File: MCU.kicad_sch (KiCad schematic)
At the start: 0 parts

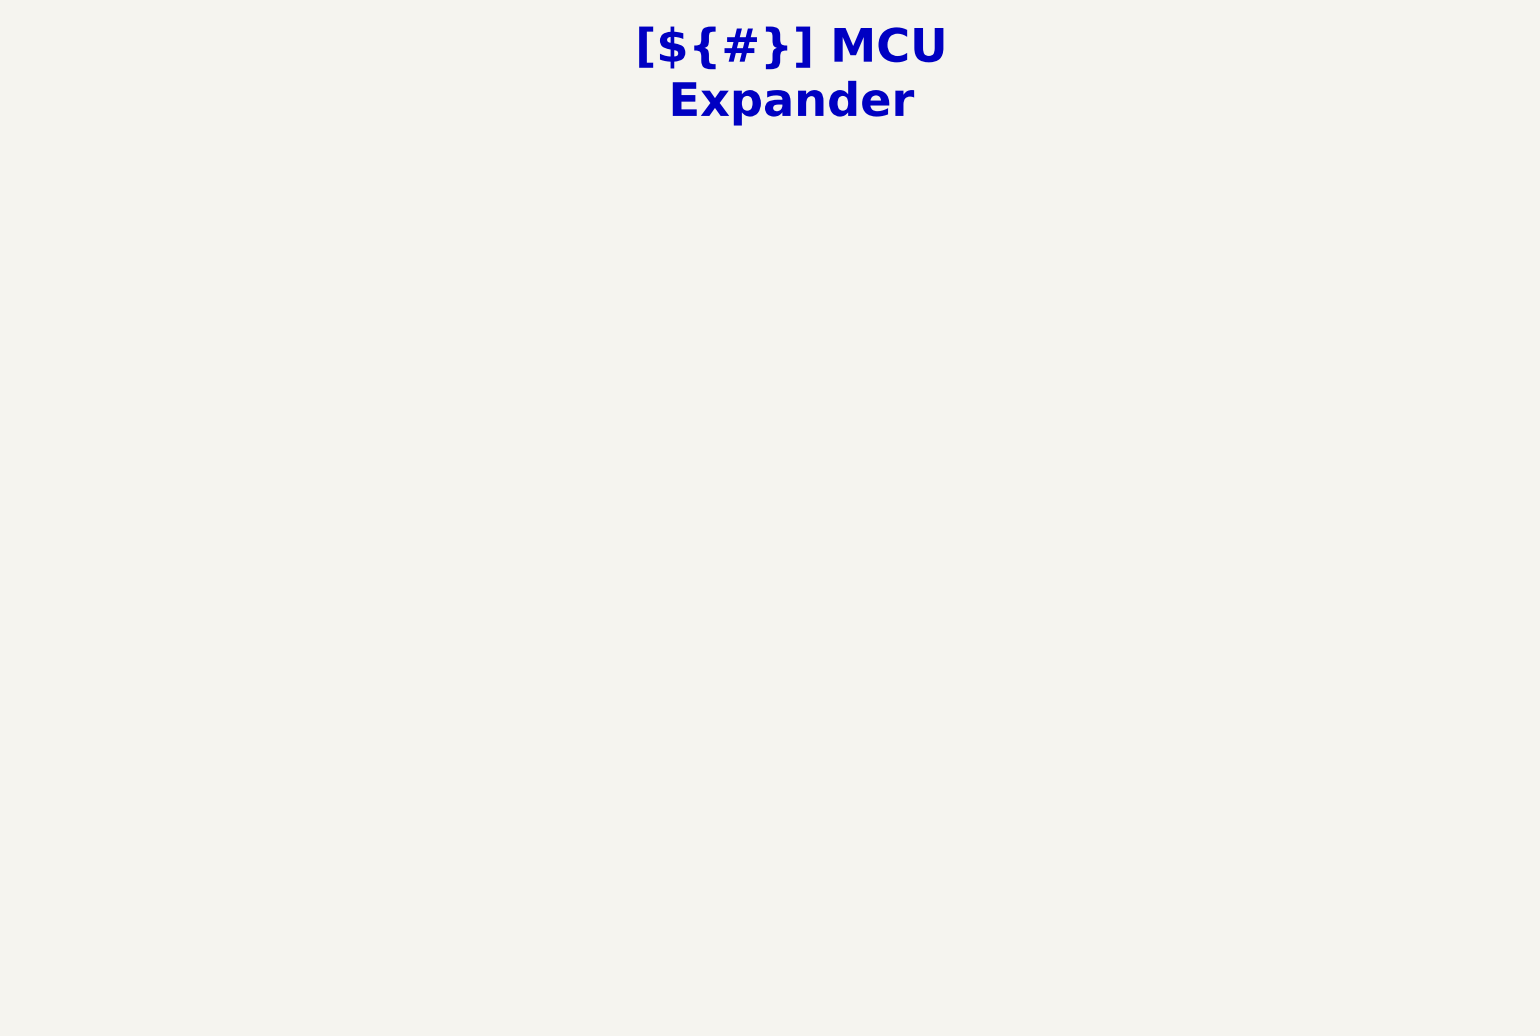
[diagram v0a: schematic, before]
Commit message: [Schematic][Add] MCU
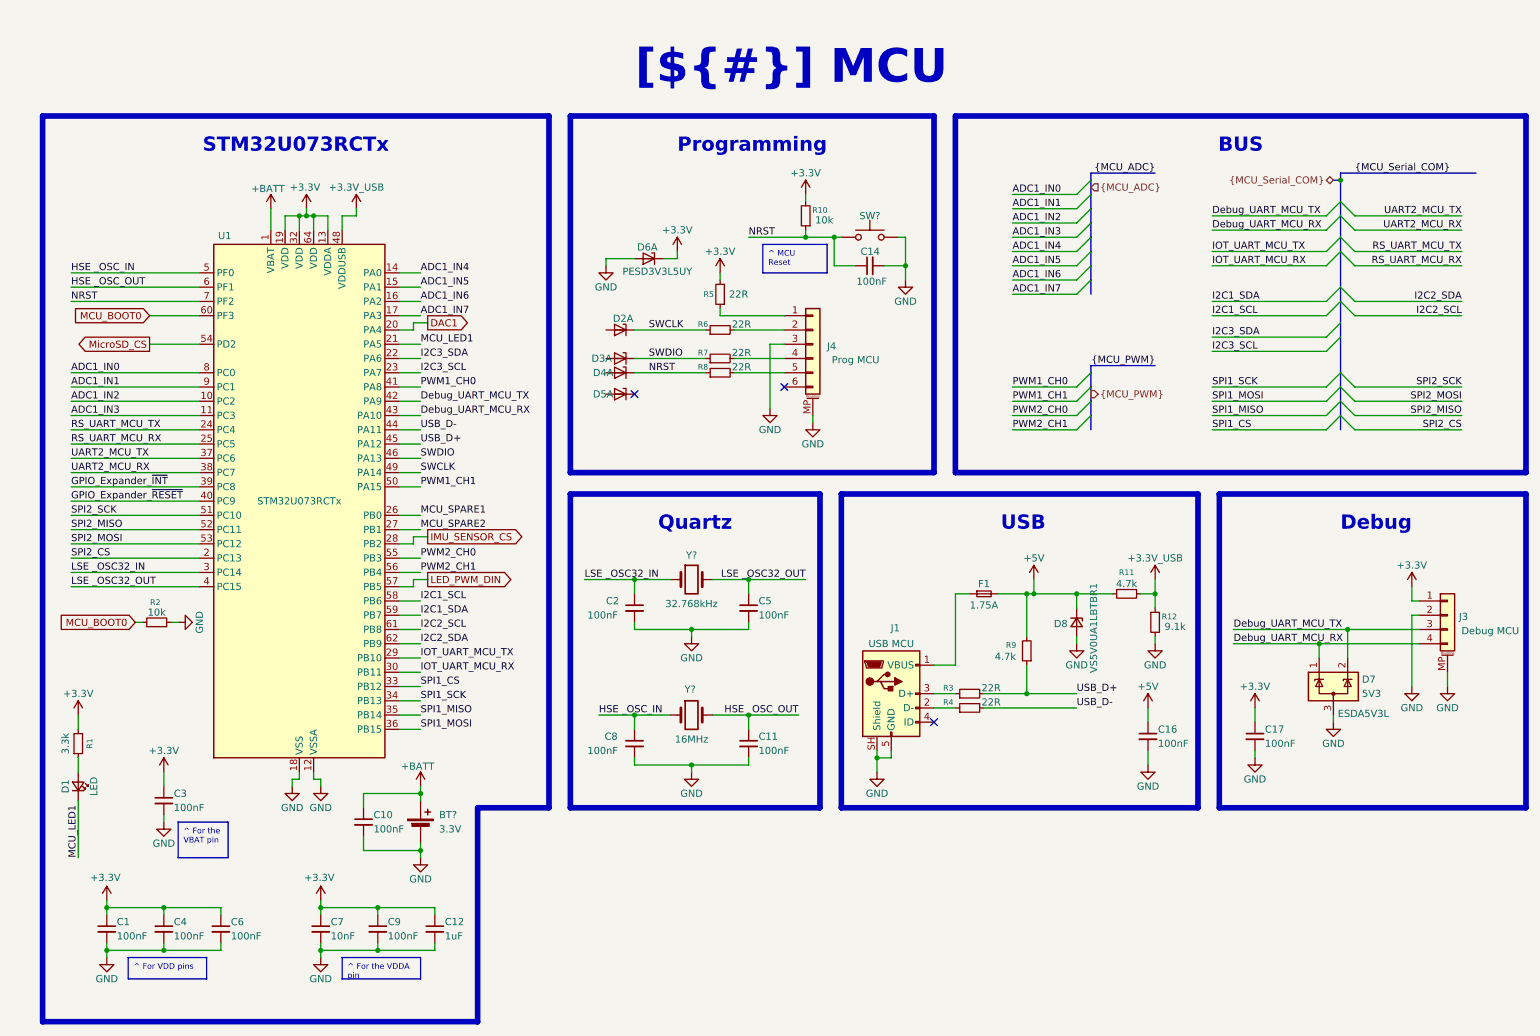
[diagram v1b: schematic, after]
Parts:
- added BT?: 3.3V, Battery:BatteryHolder_Keystone_103_1x20mm, symbol Device:Battery_Cell
- added C1, C10, C11, C14, C16, C17, C2, C3, C4, C5, C6, C8, C9: 100nF, Capacitor_SMD:C_0603_1608Metric_Pad1.08x0.95mm_HandSolder, symbol Device:C_Small
- added C12: 1uF, Capacitor_SMD:C_0603_1608Metric_Pad1.08x0.95mm_HandSolder, symbol Device:C_Small
- added C7: 10nF, Capacitor_SMD:C_0603_1608Metric_Pad1.08x0.95mm_HandSolder, symbol Device:C_Small
- added D1: 5V, LED_SMD:LED_0805_2012Metric_Pad1.15x1.40mm_HandSolder, symbol Device:LED_Small
- added D2, D3, D4, D5, D6: 3.3V, Package_TO_SOT_SMD:SOT-363_SC-70-6, symbol Power_Protection:PESD3V3L5UY
- added D7: 5V3, Package_TO_SOT_SMD:SOT-23-3, symbol Power_Protection:ESDA5V3L
- added D8: 5V, Diode_SMD:D_SMB, symbol Device:D_Zener_Small
- added F1: 1.75A, Fuse:Fuse_0603_1608Metric, symbol Device:Fuse_Small
- added J1: *, Connector_USB:USB_B_Amphenol_MUSB-D511_Vertical_Rugged, symbol Connector:USB_B_Micro
- added J3: *, Connector_JST:JST_ZH_S4B-ZR-SM4A-TF_1x04-1MP_P1.50mm_Horizontal, symbol Connector_Generic_MountingPin:Conn_01x04_MountingPin
- added J4: *, Connector_JST:JST_ZH_S6B-ZR-SM4A-TF_1x06-1MP_P1.50mm_Horizontal, symbol Connector_Generic_MountingPin:Conn_01x06_MountingPin
- added R1: 3.3k, Resistor_SMD:R_0603_1608Metric_Pad0.98x0.95mm_HandSolder, symbol Device:R_Small
- added R10, R2: 10k, Resistor_SMD:R_0603_1608Metric_Pad0.98x0.95mm_HandSolder, symbol Device:R_Small
- added R11: 4.7k, Resistor_SMD:R_0805_2012Metric_Pad1.20x1.40mm_HandSolder, symbol Device:R_Small
- added R12: 9.1k, Resistor_SMD:R_0805_2012Metric_Pad1.20x1.40mm_HandSolder, symbol Device:R_Small
- added R3, R4, R5, R6, R7, R8: 22R, Resistor_SMD:R_0603_1608Metric_Pad0.98x0.95mm_HandSolder, symbol Device:R_Small
- added R9: 4.7k, Resistor_SMD:R_0603_1608Metric_Pad0.98x0.95mm_HandSolder, symbol Device:R_Small
- added SW?: *, Button_Switch_SMD:SW_SPST_CK_RS282G05A3, symbol Switch:SW_Push
- added U1: *, Package_QFP:LQFP-64_10x10mm_P0.5mm, symbol MCU_ST_STM32U0:STM32U073RCTx
- added Y?: 32.768kHz, Crystal:Crystal_SMD_2012-2Pin_2.0x1.2mm, symbol Device:Crystal
- added Y?: 16MHz, Crystal:Crystal_SMD_2012-2Pin_2.0x1.2mm, symbol Device:Crystal
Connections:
- new net: J1.3 (D+), R3.1
- new net: J4.1 (Pin_1), R5.1
- new net: J4.2 (Pin_2), R6.2
- new net: J4.4 (Pin_4), R7.2
- new net: J4.5 (Pin_5), R8.2
- new net: D1.2 (A), R1.1
- new net: F1.1, J1.1 (VBUS)
- new net: J1.2 (D-), R4.1
- new net +3.3V: C1.1, C12.1, C17.1, C3.1, C4.1, C6.1, C7.1, C9.1, D6.1 (K1), J3.1 (Pin_1), R1.2, R10.2, R5.2, U1.13 (VDDA), U1.19 (VDD), U1.32 (VDD), U1.64 (VDD)
- new net +3.3V_USB: R11.1, R12.1, U1.48 (VDDUSB)
- new net +5V: C16.1, D8.1 (K), F1.2, R11.2, R9.2
- new net +BATT: BT?.1 (+), C10.1, U1.1 (VBAT)
- new net ADC1_IN0: U1.8 (PC0)
- new net ADC1_IN1: U1.9 (PC1)
- new net ADC1_IN2: U1.10 (PC2)
- new net ADC1_IN3: U1.11 (PC3)
- new net ADC1_IN4: U1.14 (PA0)
- new net ADC1_IN5: U1.15 (PA1)
- new net ADC1_IN6: U1.16 (PA2)
- new net ADC1_IN7: U1.17 (PA3)
- new net DAC1: U1.20 (PA4)
- new net Debug_UART_MCU_RX: D7.1 (K), J3.4 (Pin_4), U1.43 (PA10)
- new net Debug_UART_MCU_TX: D7.2 (K), J3.3 (Pin_3), U1.42 (PA9)
- new net GND: BT?.2 (-), C1.2, C10.2, C11.2, C12.2, C14.2, C16.2, C17.2, C2.2, C3.2, C4.2, C5.2, C6.2, C7.2, C8.2, C9.2, D6.2 (A), D7.3 (A), D8.2 (A), J1.5 (GND), J1.SH (Shield), J3.2 (Pin_2), J3.MP (MountPin), J4.3 (Pin_3), J4.MP (MountPin), R12.2, R2.2, SW?.2, U1.12 (VSSA), U1.18 (VSS), U1.31 (VSS), U1.47 (VSS), U1.63 (VSS)
- new net GPIO_Expander_~{INT}: U1.39 (PC8)
- new net GPIO_Expander_~{RESET}: U1.40 (PC9)
- new net HSE _OSC_IN: C8.1, U1.5 (PF0), Y?.1
- new net HSE _OSC_OUT: C11.1, U1.6 (PF1), Y?.2
- new net I2C1_SCL: U1.58 (PB6)
- new net I2C1_SDA: U1.59 (PB7)
- new net I2C2_SCL: U1.61 (PB8)
- new net I2C2_SDA: U1.62 (PB9)
- new net I2C3_SCL: U1.23 (PA7)
- new net I2C3_SDA: U1.22 (PA6)
- new net IMU_SENSOR_CS: U1.28 (PB2)
- new net IOT_UART_MCU_RX: U1.30 (PB11)
- new net IOT_UART_MCU_TX: U1.29 (PB10)
- new net LED_PWM_DIN: U1.57 (PB5)
- new net LSE _OSC32_IN: C2.1, U1.3 (PC14), Y?.1
- new net LSE _OSC32_OUT: C5.1, U1.4 (PC15), Y?.2
- new net MCU_BOOT0: R2.1, U1.60 (PF3)
- new net MCU_LED1: D1.1 (K), U1.21 (PA5)
- new net MCU_SPARE1: U1.26 (PB0)
- new net MCU_SPARE2: U1.27 (PB1)
- new net MicroSD_CS: U1.54 (PD2)
- new net NRST: C14.1, D4.1 (K1), R10.1, R8.1, SW?.1, U1.7 (PF2)
- new net PWM1_CH0: U1.41 (PA8)
- new net PWM1_CH1: U1.50 (PA15)
- new net PWM2_CH0: U1.55 (PB3)
- new net PWM2_CH1: U1.56 (PB4)
- new net RS_UART_MCU_RX: U1.25 (PC5)
- new net RS_UART_MCU_TX: U1.24 (PC4)
- new net SPI1_CS: U1.33 (PB12)
- new net SPI1_MISO: U1.35 (PB14)
- new net SPI1_MOSI: U1.36 (PB15)
- new net SPI1_SCK: U1.34 (PB13)
- new net SPI2_CS: U1.2 (PC13)
- new net SPI2_MISO: U1.52 (PC11)
- new net SPI2_MOSI: U1.53 (PC12)
- new net SPI2_SCK: U1.51 (PC10)
- new net SWCLK: D2.1 (K1), R6.1, U1.49 (PA14)
- new net SWDIO: D3.1 (K1), R7.1, U1.46 (PA13)
- new net UART2_MCU_RX: U1.38 (PC7)
- new net UART2_MCU_TX: U1.37 (PC6)
- new net USB_D+: R3.2, R9.1, U1.45 (PA12)
- new net USB_D-: R4.2, U1.44 (PA11)
- no-connect marks 0 -> 3
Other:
- title: MCU Expander -> MCU

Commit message: [Schematic][Add] MCU Expander Schematic
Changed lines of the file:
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@@
 	(wire
 		(pts
+			(xy 82.55 100.33) (xy 82.55 99.06)
+		)
+		(stroke
+			(width 0)
+			(type default)
+		)
+	)
+	(wire
+		(pts
 			(xy 121.92 135.89) (xy 121.92 138.43)
 		)
@@
 	(wire
 		(pts
+			(xy 43.18 95.25) (xy 44.45 95.25)
+		)
+		(stroke
+			(width 0)
+			(type default)
+		)
+	)
+	(wire
+		(pts
 			(xy 250.19 55.88) (xy 269.24 55.88)
 		)
@@
 	(wire
 		(pts
+			(xy 82.55 102.87) (xy 82.55 101.6)
+		)
+		(stroke
+			(width 0)
+			(type default)
+		)
+	)
+	(wire
+		(pts
 			(xy 170.18 50.8) (xy 168.91 50.8)
 		)
@@
 	(wire
 		(pts
+			(xy 82.55 101.6) (xy 85.09 101.6)
+		)
+		(stroke
+			(width 0)
+			(type default)
+		)
+	)
+	(wire
+		(pts
 			(xy 260.35 113.03) (xy 260.35 115.57)
 		)
@@
 	(wire
 		(pts
+			(xy 82.55 99.06) (xy 85.09 99.06)
+		)
+		(stroke
+			(width 0)
+			(type default)
+		)
+	)
+	(wire
+		(pts
+			(xy 41.91 93.98) (xy 43.18 93.98)
+		)
+		(stroke
+			(width 0)
+			(type default)
+		)
+	)
+	(wire
+		(pts
 			(xy 80.01 128.27) (xy 83.82 128.27)
 		)
@@
 	(wire
 		(pts
-			(xy 21.59 97.79) (xy 44.45 97.79)
+			(xy 41.91 96.52) (xy 43.18 96.52)
 		)
 		(stroke
@@
 	(wire
 		(pts
+			(xy 43.18 93.98) (xy 43.18 95.25)
+		)
+		(stroke
+			(width 0)
+			(type default)
+		)
+	)
+	(wire
+		(pts
 			(xy 38.1 170.18) (xy 38.1 171.45)
 		)
@@
 	(wire
 		(pts
+			(xy 43.18 97.79) (xy 44.45 97.79)
+		)
+		(stroke
+			(width 0)
+			(type default)
+		)
+	)
+	(wire
+		(pts
 			(xy 116.84 54.61) (xy 116.84 55.88)
 		)
@@
 	(wire
 		(pts
-			(xy 80.01 102.87) (xy 83.82 102.87)
+			(xy 80.01 102.87) (xy 82.55 102.87)
 		)
 		(stroke
@@
 	(wire
 		(pts
-			(xy 21.59 95.25) (xy 44.45 95.25)
-		)
-		(stroke
-			(width 0)
-			(type default)
-		)
-	)
-	(wire
-		(pts
 			(xy 66.04 168.91) (xy 66.04 170.18)
 		)
@@
 	(wire
 		(pts
-			(xy 80.01 100.33) (xy 83.82 100.33)
+			(xy 80.01 100.33) (xy 82.55 100.33)
 		)
 		(stroke
@@
 	(wire
 		(pts
+			(xy 43.18 96.52) (xy 43.18 97.79)
+		)
+		(stroke
+			(width 0)
+			(type default)
+		)
+	)
+	(wire
+		(pts
 			(xy 152.4 43.18) (xy 152.4 44.45)
 		)
@@
 		)
 	)
-	(label "GPIO_Expander_~{INT}"
-		(at 21.59 95.25 0)
-		(effects
-			(font
-				(size 1.27 1.27)
-			)
-			(justify left bottom)
-		)
-	)
 	(label "Debug_UART_MCU_TX"
 		(at 224.79 46.99 0)
@@
 		)
 	)
-	(label "GPIO_Expander_~{RESET}"
-		(at 21.59 97.79 0)
-		(effects
-			(font
-				(size 1.27 1.27)
-			)
-			(justify left bottom)
-		)
-	)
 	(label "SPI2_MOSI"
 		(at 21.59 105.41 0)
@@
 		)
 	)
-	(label "MCU_SPARE1"
-		(at 83.82 100.33 0)
-		(effects
-			(font
-				(size 1.27 1.27)
-			)
-			(justify left bottom)
-		)
-	)
 	(label "SPI2_SCK"
 		(at 269.24 77.47 180)
@@
 		)
 	)
-	(label "MCU_SPARE2"
-		(at 83.82 102.87 0)
-		(effects
-			(font
-				(size 1.27 1.27)
-			)
-			(justify left bottom)
-		)
-	)
 	(label "I2C3_SCL"
 		(at 83.82 74.93 0)
@@
 		)
 	)
+	(global_label "GPIO_Expander_~{INT}"
+		(shape input)
+		(at 41.91 93.98 180)
+		(fields_autoplaced yes)
+		(effects
+			(font
+				(size 1.27 1.27)
+			)
+			(justify right)
+		)
+		(property "Intersheetrefs" "${INTERSHEET_REFS}"
+			(at 20.9635 93.98 0)
+			(effects
+				(font
+					(size 1.27 1.27)
+				)
+				(justify right)
+				(hide yes)
+			)
+		)
+	)
+	(global_label "MCU_SPARE1"
+		(shape bidirectional)
+		(at 85.09 99.06 0)
+		(fields_autoplaced yes)
+		(effects
+			(font
+				(size 1.27 1.27)
+			)
+			(justify left)
+		)
+		(property "Intersheetrefs" "${INTERSHEET_REFS}"
+			(at 100.2913 99.06 0)
+			(effects
+				(font
+					(size 1.27 1.27)
+				)
+				(justify left)
+				(hide yes)
+			)
+		)
+	)
 	(global_label "MCU_BOOT0"
 		(shape input)
@@
 		)
 	)
+	(global_label "GPIO_Expander_~{RESET}"
+		(shape input)
+		(at 41.91 96.52 180)
+		(fields_autoplaced yes)
+		(effects
+			(font
+				(size 1.27 1.27)
+			)
+			(justify right)
+		)
+		(property "Intersheetrefs" "${INTERSHEET_REFS}"
+			(at 18.1213 96.52 0)
+			(effects
+				(font
+					(size 1.27 1.27)
+				)
+				(justify right)
+				(hide yes)
+			)
+		)
+	)
 	(global_label "DAC1"
 		(shape output)
@@
 			(effects
 				(font
+					(size 1.27 1.27)
+				)
+				(justify left)
+				(hide yes)
+			)
+		)
+	)
+	(global_label "MCU_SPARE2"
+		(shape bidirectional)
+		(at 85.09 101.6 0)
+		(fields_autoplaced yes)
+		(effects
+			(font
+				(size 1.27 1.27)
+			)
+			(justify left)
+		)
+		(property "Intersheetrefs" "${INTERSHEET_REFS}"
+			(at 101.4026 101.6 0)
+			(effects
+				(font

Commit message: [Schematic][Modify] Clear all annotation
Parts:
- renumbered C4 to C?, C1 to C?, C10 to C?, C17 to C?, C8 to C?, C16 to C?, C12 to C?, C14 to C?, C11 to C?, C6 to C?, C2 to C?, C3 to C?, C5 to C?, C9 to C?, C7 to C?, D4 to D?, D7 to D?, D8 to D?, D3 to D?, D6 to D?, D5 to D?, D2 to D?, D1 to D?, F1 to F?, J4 to J?, J3 to J?, J1 to J?, R3 to R?, R5 to R?, R1 to R?, R4 to R?, R9 to R?, R10 to R?, R11 to R?, R7 to R?, R6 to R?, R12 to R?, R2 to R?, R8 to R?, U1 to U?

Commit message: [Schematic][Modify] Modification of the TVD programming Diode
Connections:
- net NRST: now also D?.5 (K4); no longer D?.1 (K1)
- net SWCLK: now also D?.3 (K2); no longer D?.1 (K1)
- net SWDIO: now also D?.4 (K3); no longer D?.1 (K1)
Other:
- moved on the sheet: D?A
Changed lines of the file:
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@@
 		(exclude_from_sim no)
 		(at 227.33 97.6497 0)
-		(size 53.34 7.7603)
+		(size 52.07 7.7603)
 		(margins 1.9049 1.9049 1.9049 1.9049)
 		(stroke
@@
 	(wire
 		(pts
-			(xy 129.54 54.61) (xy 129.54 53.34)
-		)
-		(stroke
-			(width 0)
-			(type default)
-		)
-	)
-	(wire
-		(pts
 			(xy 80.01 118.11) (xy 83.82 118.11)
 		)
@@
 	(wire
 		(pts
-			(xy 121.92 54.61) (xy 116.84 54.61)
+			(xy 118.11 53.34) (xy 118.11 57.15)
 		)
 		(stroke
@@
 	(wire
 		(pts
-			(xy 127 54.61) (xy 129.54 54.61)
+			(xy 118.11 48.26) (xy 118.11 44.45)
 		)
 		(stroke
@@
 	(wire
 		(pts
-			(xy 116.84 54.61) (xy 116.84 55.88)
-		)
-		(stroke
-			(width 0)
-			(type default)
-		)
-	)
-	(wire
-		(pts
 			(xy 165.1 143.51) (xy 165.1 146.05)
 		)
@@
 		(lib_id "Power_Protection:PESD3V3L5UY")
 		(at 119.38 74.93 180)
-		(unit 1)
+		(unit 4)
 		(exclude_from_sim no)
 		(in_bom yes)
@@
 		(dnp no)
 		(property "Reference" "D?"
-			(at 116.332 74.93 0)
+			(at 116.078 74.93 0)
 			(effects
 				(font
@@
 				(path "/f9e05184-c88b-4a88-ae9c-ab2bdb32be7c/c5103ceb-5325-4a84-a025-9638a412984e/8566d017-436e-49aa-b68c-18b49ef4128b"
 					(reference "D?")
-					(unit 1)
+					(unit 4)
 				)
 			)
@@
 		(lib_id "Power_Protection:PESD3V3L5UY")
 		(at 119.38 72.39 180)
-		(unit 1)
+		(unit 3)
 		(exclude_from_sim no)
 		(in_bom yes)
@@
 				(path "/f9e05184-c88b-4a88-ae9c-ab2bdb32be7c/c5103ceb-5325-4a84-a025-9638a412984e/8566d017-436e-49aa-b68c-18b49ef4128b"
 					(reference "D?")
-					(unit 1)
+					(unit 3)
 				)
 			)
@@
 		(dnp no)
 		(property "Reference" "C?"
-			(at 165.608 53.34 90)
+			(at 165.1 53.086 90)
 			(effects
 				(font
@@
 	(symbol
 		(lib_id "power:+3.3V")
-		(at 129.54 53.34 0)
+		(at 118.11 44.45 0)
 		(unit 1)
 		(exclude_from_sim no)
@@
 		(dnp no)
 		(property "Reference" "#PWR?"
-			(at 129.54 57.15 0)
+			(at 118.11 48.26 0)
 			(effects
 				(font
@@
 		)
 		(property "Value" "+3.3V"
-			(at 129.54 49.53 0)
+			(at 118.11 40.64 0)
 			(effects
 				(font
@@
 		)
 		(property "Footprint" ""
-			(at 129.54 53.34 0)
+			(at 118.11 44.45 0)
 			(effects
 				(font
@@
 		)
 		(property "Datasheet" ""
-			(at 129.54 53.34 0)
+			(at 118.11 44.45 0)
 			(effects
 				(font
@@
 		)
 		(property "Description" "Power symbol creates a global label with name \"+3.3V\""
-			(at 129.54 53.34 0)
+			(at 118.11 44.45 0)
 			(effects
 				(font
@@
 	(symbol
 		(lib_id "Power_Protection:PESD3V3L5UY")
-		(at 124.46 54.61 180)
+		(at 118.11 50.8 270)
 		(unit 1)
 		(exclude_from_sim no)
@@
 		(dnp no)
 		(property "Reference" "D?"
-			(at 124.206 52.578 0)
+			(at 116.078 51.054 0)
 			(effects
 				(font
@@
 		)
 		(property "Value" "3.3V"
-			(at 124.46 50.8 0)
+			(at 114.3 50.8 0)
 			(effects
 				(font
@@
 		)
 		(property "Footprint" "Package_TO_SOT_SMD:SOT-363_SC-70-6"
-			(at 124.46 59.69 0)
+			(at 123.19 50.8 0)
 			(effects
 				(font
@@
 		)
 		(property "Datasheet" "https://assets.nexperia.com/documents/data-sheet/PESDXL5UF_V_Y.pdf"
-			(at 124.46 49.53 0)
+			(at 113.03 50.8 0)
 			(effects
 				(font
@@
 		)
 		(property "Description" "Low capacitance unidirectional fivefold ESD protection diode array, 3.3V, Common Anode, SOT-363"
-			(at 124.46 54.61 0)
+			(at 118.11 50.8 0)
 			(effects
 				(font
@@
 		)
 		(property "PartNumber" "PESD3V3L5UY"
-			(at 125.984 56.896 0)
+			(at 120.396 49.276 0)
 			(effects
 				(font
@@
 		)
 		(property "PackageReference" "SOT-363"
-			(at 124.46 54.61 0)
+			(at 118.11 50.8 0)
 			(effects
 				(font
@@
 		)
 		(property "Manufacturer" "Nexperia"
-			(at 124.46 54.61 0)
+			(at 118.11 50.8 0)
 			(effects
 				(font
@@
 		)
 		(property "Comment" "ESD Diode"
-			(at 124.46 54.61 0)
+			(at 118.11 50.8 0)
 			(effects
 				(font
@@
 		(lib_id "Power_Protection:PESD3V3L5UY")
 		(at 119.38 78.74 180)
-		(unit 1)
+		(unit 5)
 		(exclude_from_sim no)
 		(in_bom yes)
@@
 		(dnp no)
 		(property "Reference" "D?"
-			(at 116.332 78.74 0)
+			(at 116.078 78.74 0)
 			(effects
 				(font
@@
 				(path "/f9e05184-c88b-4a88-ae9c-ab2bdb32be7c/c5103ceb-5325-4a84-a025-9638a412984e/8566d017-436e-49aa-b68c-18b49ef4128b"
 					(reference "D?")
-					(unit 1)
+					(unit 5)
 				)
 			)
@@
 		(lib_id "Power_Protection:PESD3V3L5UY")
 		(at 119.38 67.31 180)
-		(unit 1)
+		(unit 2)
 		(exclude_from_sim no)
 		(in_bom yes)
@@
 		(dnp no)
 		(property "Reference" "D?"
-			(at 119.888 65.278 0)
+			(at 116.078 67.31 0)
 			(effects
 				(font
@@
 				(path "/f9e05184-c88b-4a88-ae9c-ab2bdb32be7c/c5103ceb-5325-4a84-a025-9638a412984e/8566d017-436e-49aa-b68c-18b49ef4128b"
 					(reference "D?")
-					(unit 1)
+					(unit 2)
 				)
 			)
@@
 	(symbol
 		(lib_id "power:GND")
-		(at 116.84 55.88 0)
+		(at 118.11 57.15 0)
 		(unit 1)
 		(exclude_from_sim no)
@@
 		(dnp no)
 		(property "Reference" "#PWR?"
-			(at 116.84 62.23 0)
+			(at 118.11 63.5 0)
 			(effects
 				(font
@@
 		)
 		(property "Value" "GND"
-			(at 116.84 59.69 0)
+			(at 118.11 60.96 0)
 			(effects
 				(font
@@
 		)
 		(property "Footprint" ""
-			(at 116.84 55.88 0)
+			(at 118.11 57.15 0)
 			(effects
 				(font
@@
 		)
 		(property "Datasheet" ""
-			(at 116.84 55.88 0)
+			(at 118.11 57.15 0)
 			(effects
 				(font
@@
 		)
 		(property "Description" "Power symbol creates a global label with name \"GND\" , ground"
-			(at 116.84 55.88 0)
+			(at 118.11 57.15 0)
 			(effects
 				(font

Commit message: [Schematic][Modify] Annotation of all  the components
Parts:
- gave numbers to parts that had none: 40

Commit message: [Schematic][Modify] Annotation of all  the components
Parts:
- renumbered C13 to C1, C1 to C10, C3 to C11, C4 to C12, C5 to C13, C7 to C14, C8 to C15, C9 to C2, C11 to C3, C14 to C4, C15 to C5, C10 to C6, C12 to C7, C2 to C8, C6 to C9, D2 to D1, D3 to D2, D4 to D3, D1 to D4, J3 to J2, J2 to J3, R7 to R1, R8 to R10, R9 to R11, R1 to R12, R3 to R2, R4 to R3, R5 to R4, R6 to R5, R11 to R6, R2 to R7, R12 to R8, R10 to R9
